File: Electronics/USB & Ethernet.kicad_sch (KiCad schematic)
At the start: 13 parts, among them IC4 USB2512B-AEZG, J24 USB_A_Stacked, Y3 30MHz

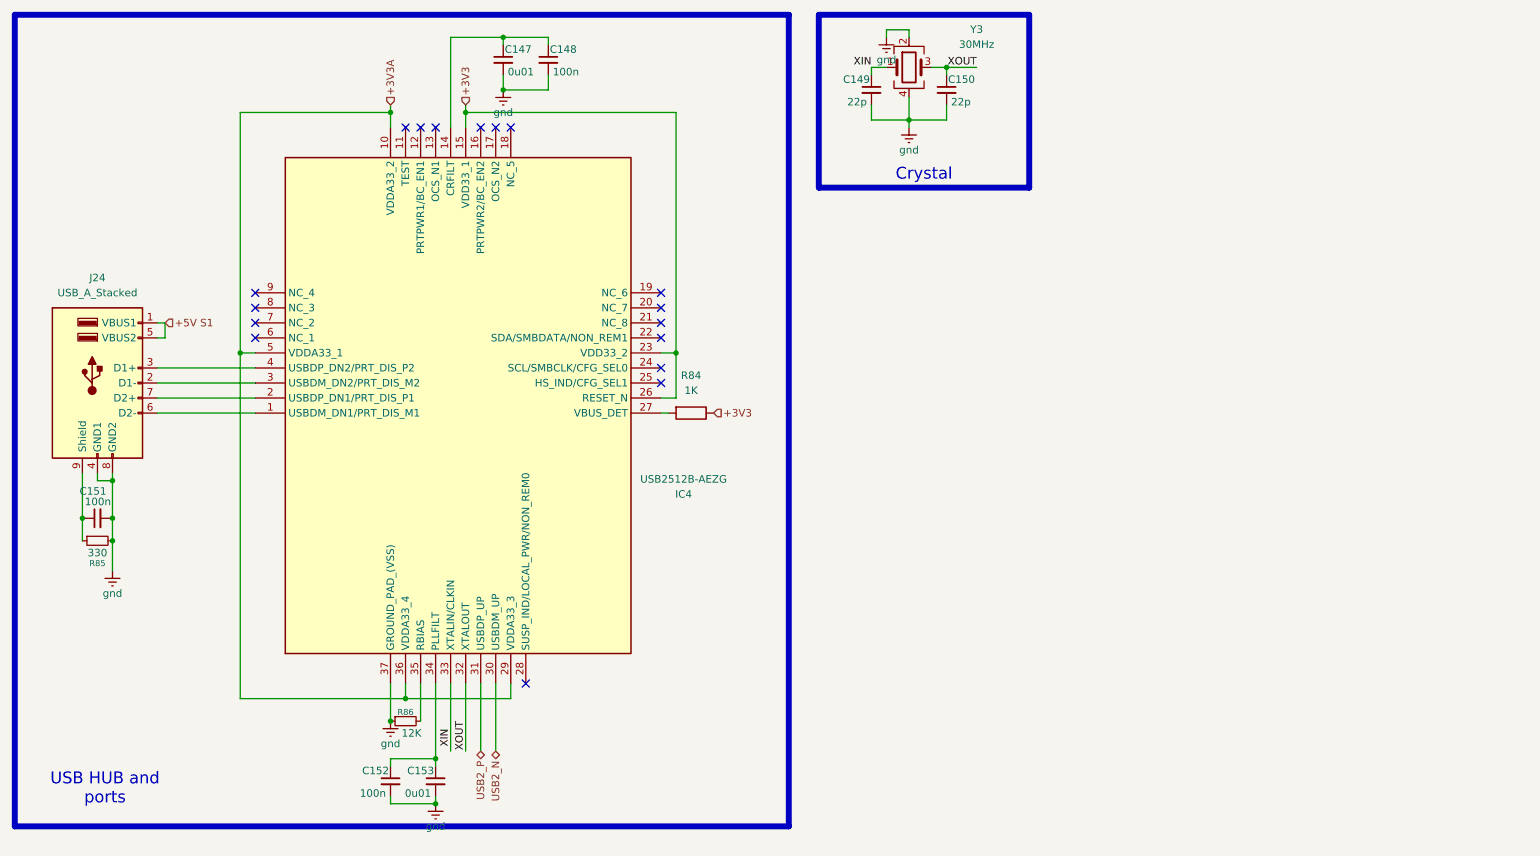
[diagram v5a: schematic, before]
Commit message: Sata Port Changed
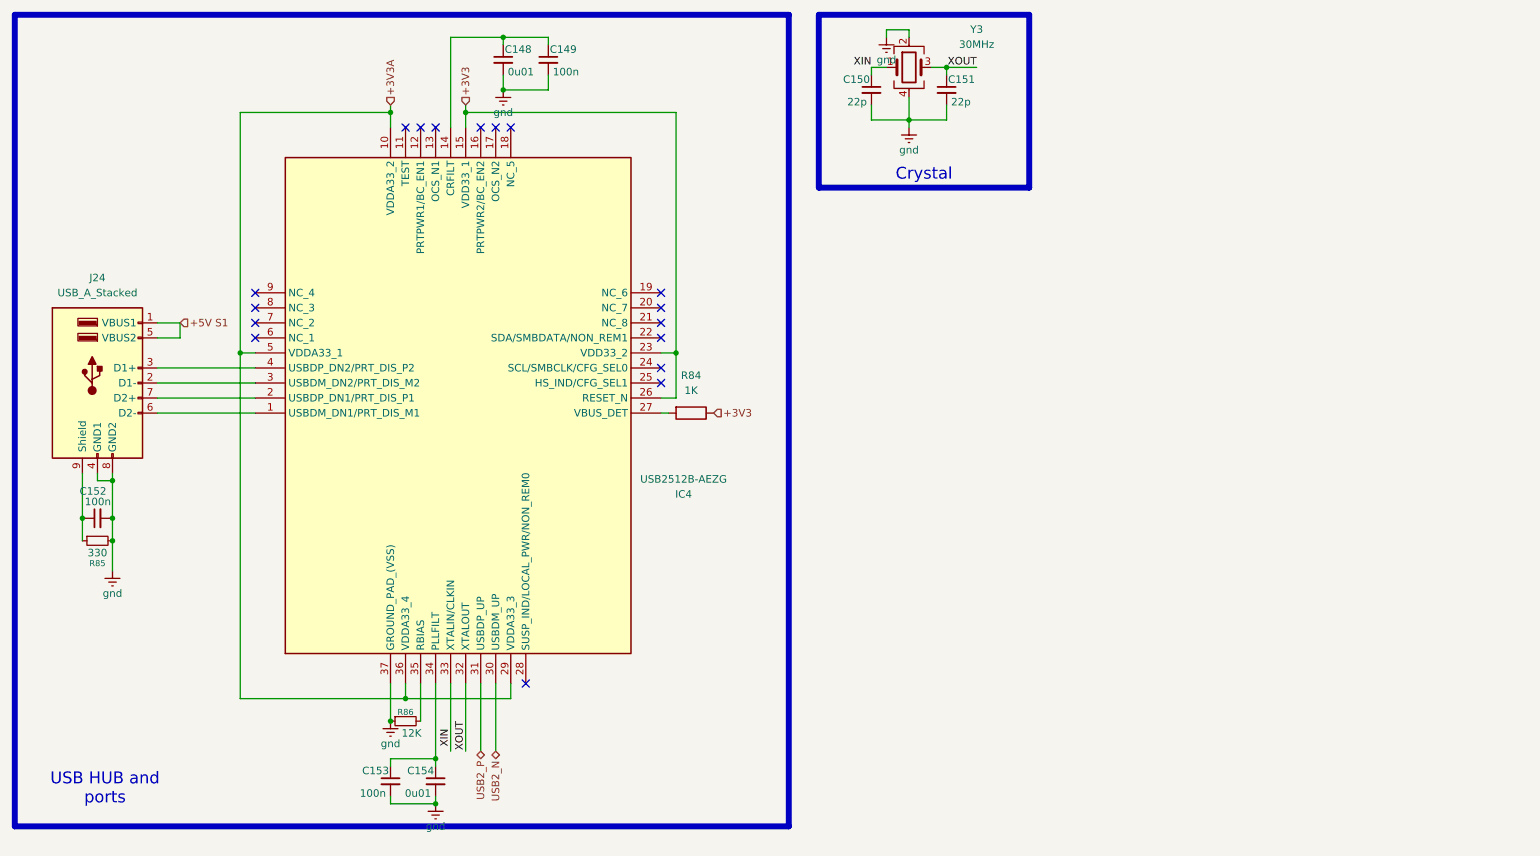
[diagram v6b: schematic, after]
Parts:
- renumbered C147 to C148, C148 to C149, C149 to C150, C150 to C151, C151 to C152, C152 to C153, C153 to C154
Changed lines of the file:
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@@
 	(wire
 		(pts
-			(xy 39.37 69.85) (xy 40.64 69.85)
+			(xy 43.18 69.85) (xy 43.18 67.31)
+		)
+		(stroke
+			(width 0)
+			(type default)
+		)
+	)
+	(wire
+		(pts
+			(xy 39.37 69.85) (xy 43.18 69.85)
 		)
 		(stroke
@@
 	(wire
 		(pts
-			(xy 40.64 67.31) (xy 39.37 67.31)
-		)
-		(stroke
-			(width 0)
-			(type default)
-		)
-	)
-	(wire
-		(pts
 			(xy 166.37 33.02) (xy 172.72 33.02)
 		)
@@
 	(wire
 		(pts
-			(xy 40.64 69.85) (xy 40.64 67.31)
-		)
-		(stroke
-			(width 0)
-			(type default)
-		)
-	)
-	(wire
-		(pts
 			(xy 88.9 128.27) (xy 88.9 139.7)
 		)
@@
 		(pts
 			(xy 97.79 25.4) (xy 97.79 27.94)
+		)
+		(stroke
+			(width 0)
+			(type default)
+		)
+	)
+	(wire
+		(pts
+			(xy 43.18 67.31) (xy 39.37 67.31)
 		)
 		(stroke
@@
 	(hierarchical_label "+5V S1"
 		(shape input)
-		(at 40.64 67.31 0)
+		(at 43.18 67.31 0)
 		(effects
 			(font
@@
 			)
 			(justify right)
+		)
+	)
+	(netclass_flag ""
+		(length 2.54)
+		(shape round)
+		(at 53.34 31.75 0)
+		(fields_autoplaced yes)
+		(effects
+			(font
+				(size 1.27 1.27)
+			)
+			(justify left bottom)
+		)
+		(property "Netclass" "PWR RAIL"
+			(at 54.0385 29.21 0)
+			(effects
+				(font
+					(size 1.27 1.27)
+				)
+				(justify left)
+			)
+		)
+		(property "Component Class" ""
+			(at -344.17 -53.34 0)
+			(effects
+				(font
+					(size 1.27 1.27)
+					(italic yes)
+				)
+			)
+		)
+	)
+	(netclass_flag ""
+		(length 2.54)
+		(shape round)
+		(at 43.18 69.85 180)
+		(fields_autoplaced yes)
+		(effects
+			(font
+				(size 1.27 1.27)
+			)
+			(justify right bottom)
+		)
+		(property "Netclass" "PWR RAIL"
+			(at 43.8785 72.39 0)
+			(effects
+				(font
+					(size 1.27 1.27)
+				)
+				(justify left)
+			)
+		)
+		(property "Component Class" ""
+			(at -354.33 154.94 0)
+			(effects
+				(font
+					(size 1.27 1.27)
+					(italic yes)
+				)
+			)
+		)
+	)
+	(netclass_flag ""
+		(length 2.54)
+		(shape round)
+		(at 127 31.75 0)
+		(fields_autoplaced yes)
+		(effects
+			(font
+				(size 1.27 1.27)
+			)
+			(justify left bottom)
+		)
+		(property "Netclass" "PWR RAIL"
+			(at 126.3015 29.21 0)
+			(effects
+				(font
+					(size 1.27 1.27)
+				)
+				(justify right)
+			)
+		)
+		(property "Component Class" ""
+			(at 524.51 -53.34 0)
+			(effects
+				(font
+					(size 1.27 1.27)
+					(italic yes)
+				)
+				(justify left)
+			)
 		)
 	)
@@
 		(on_board yes)
 		(dnp no)
-		(property "Reference" "#PWR0167"
+		(property "Reference" "#PWR0169"
 			(at 97.79 34.29 0)
 			(effects
@@
 			(project "CM5 Nas"
 				(path "/0650c7a8-acba-429c-9f8e-eec0baf0bc1c/fede4c36-00cc-4d3d-b71c-5243ba232202/6a9d58eb-7efc-489b-8392-0909cd6b0d5f"
-					(reference "#PWR0167")
+					(reference "#PWR0169")
 					(unit 1)
 				)
@@
 		(on_board yes)
 		(dnp no)
-		(property "Reference" "C153"
+		(property "Reference" "C154"
 			(at 86.106 143.002 0)
 			(effects
@@
 			(project "CM5 Nas"
 				(path "/0650c7a8-acba-429c-9f8e-eec0baf0bc1c/fede4c36-00cc-4d3d-b71c-5243ba232202/6a9d58eb-7efc-489b-8392-0909cd6b0d5f"
-					(reference "C153")
+					(reference "C154")
 					(unit 1)
 				)
@@
 		(on_board yes)
 		(dnp no)
-		(property "Reference" "C152"
+		(property "Reference" "C153"
 			(at 78.486 143.002 0)
 			(effects
@@
 			(project "CM5 Nas"
 				(path "/0650c7a8-acba-429c-9f8e-eec0baf0bc1c/fede4c36-00cc-4d3d-b71c-5243ba232202/6a9d58eb-7efc-489b-8392-0909cd6b0d5f"
-					(reference "C152")
+					(reference "C153")
 					(unit 1)
 				)
@@
 		(on_board yes)
 		(dnp no)
-		(property "Reference" "C150"
+		(property "Reference" "C151"
 			(at 172.974 26.162 0)
 			(effects
@@
 			(project "CM5 Nas"
 				(path "/0650c7a8-acba-429c-9f8e-eec0baf0bc1c/fede4c36-00cc-4d3d-b71c-5243ba232202/6a9d58eb-7efc-489b-8392-0909cd6b0d5f"
-					(reference "C150")
+					(reference "C151")
 					(unit 1)
 				)
@@
 		(on_board yes)
 		(dnp no)
-		(property "Reference" "C147"
+		(property "Reference" "C148"
 			(at 98.044 21.082 0)
 			(effects
@@
 			(project "CM5 Nas"
 				(path "/0650c7a8-acba-429c-9f8e-eec0baf0bc1c/fede4c36-00cc-4d3d-b71c-5243ba232202/6a9d58eb-7efc-489b-8392-0909cd6b0d5f"
-					(reference "C147")
+					(reference "C148")
 					(unit 1)
 				)
@@
 		(on_board yes)
 		(dnp no)
-		(property "Reference" "#PWR0166"
+		(property "Reference" "#PWR0168"
 			(at 162.56 25.4 0)
 			(effects
@@
 			(project "CM5 Nas"
 				(path "/0650c7a8-acba-429c-9f8e-eec0baf0bc1c/fede4c36-00cc-4d3d-b71c-5243ba232202/6a9d58eb-7efc-489b-8392-0909cd6b0d5f"
-					(reference "#PWR0166")
+					(reference "#PWR0168")
 					(unit 1)
 				)
@@
 		(on_board yes)
 		(dnp no)
-		(property "Reference" "#PWR0168"
+		(property "Reference" "#PWR0170"
 			(at 166.37 40.64 0)
 			(effects
@@
 			(project "CM5 Nas"
 				(path "/0650c7a8-acba-429c-9f8e-eec0baf0bc1c/fede4c36-00cc-4d3d-b71c-5243ba232202/6a9d58eb-7efc-489b-8392-0909cd6b0d5f"
-					(reference "#PWR0168")
+					(reference "#PWR0170")
 					(unit 1)
 				)
@@
 		(on_board yes)
 		(dnp no)
-		(property "Reference" "#PWR0171"
+		(property "Reference" "#PWR0173"
 			(at 86.36 154.94 0)
 			(effects
@@
 			(project "CM5 Nas"
 				(path "/0650c7a8-acba-429c-9f8e-eec0baf0bc1c/fede4c36-00cc-4d3d-b71c-5243ba232202/6a9d58eb-7efc-489b-8392-0909cd6b0d5f"
-					(reference "#PWR0171")
+					(reference "#PWR0173")
 					(unit 1)
 				)
@@
 		(on_board yes)
 		(dnp no)
-		(property "Reference" "C148"
+		(property "Reference" "C149"
 			(at 105.664 21.082 0)
 			(effects
@@
 			(project "CM5 Nas"
 				(path "/0650c7a8-acba-429c-9f8e-eec0baf0bc1c/fede4c36-00cc-4d3d-b71c-5243ba232202/6a9d58eb-7efc-489b-8392-0909cd6b0d5f"
-					(reference "C148")
+					(reference "C149")
 					(unit 1)
 				)
@@
 		(on_board yes)
 		(dnp no)
-		(property "Reference" "#PWR0169"
+		(property "Reference" "#PWR0171"
 			(at 31.75 115.57 0)
 			(effects
@@
 			(project "CM5 Nas"
 				(path "/0650c7a8-acba-429c-9f8e-eec0baf0bc1c/fede4c36-00cc-4d3d-b71c-5243ba232202/6a9d58eb-7efc-489b-8392-0909cd6b0d5f"
-					(reference "#PWR0169")
+					(reference "#PWR0171")
 					(unit 1)
 				)
@@
 		(on_board yes)
 		(dnp no)
-		(property "Reference" "#PWR0170"
+		(property "Reference" "#PWR0172"
 			(at 78.74 140.97 0)
 			(effects
@@
 			(project "CM5 Nas"
 				(path "/0650c7a8-acba-429c-9f8e-eec0baf0bc1c/fede4c36-00cc-4d3d-b71c-5243ba232202/6a9d58eb-7efc-489b-8392-0909cd6b0d5f"
-					(reference "#PWR0170")
+					(reference "#PWR0172")
 					(unit 1)
 				)
@@
 		(on_board yes)
 		(dnp no)
-		(property "Reference" "C151"
+		(property "Reference" "C152"
 			(at 30.734 95.758 90)
 			(effects
@@
 			(project "CM5 Nas"
 				(path "/0650c7a8-acba-429c-9f8e-eec0baf0bc1c/fede4c36-00cc-4d3d-b71c-5243ba232202/6a9d58eb-7efc-489b-8392-0909cd6b0d5f"
-					(reference "C151")
+					(reference "C152")
 					(unit 1)
 				)
@@
 		(on_board yes)
 		(dnp no)
-		(property "Reference" "C149"
+		(property "Reference" "C150"
 			(at 159.766 26.162 0)
 			(effects
@@
 			(project "CM5 Nas"
 				(path "/0650c7a8-acba-429c-9f8e-eec0baf0bc1c/fede4c36-00cc-4d3d-b71c-5243ba232202/6a9d58eb-7efc-489b-8392-0909cd6b0d5f"
-					(reference "C149")
+					(reference "C150")
 					(unit 1)
 				)

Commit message: Changed sata port
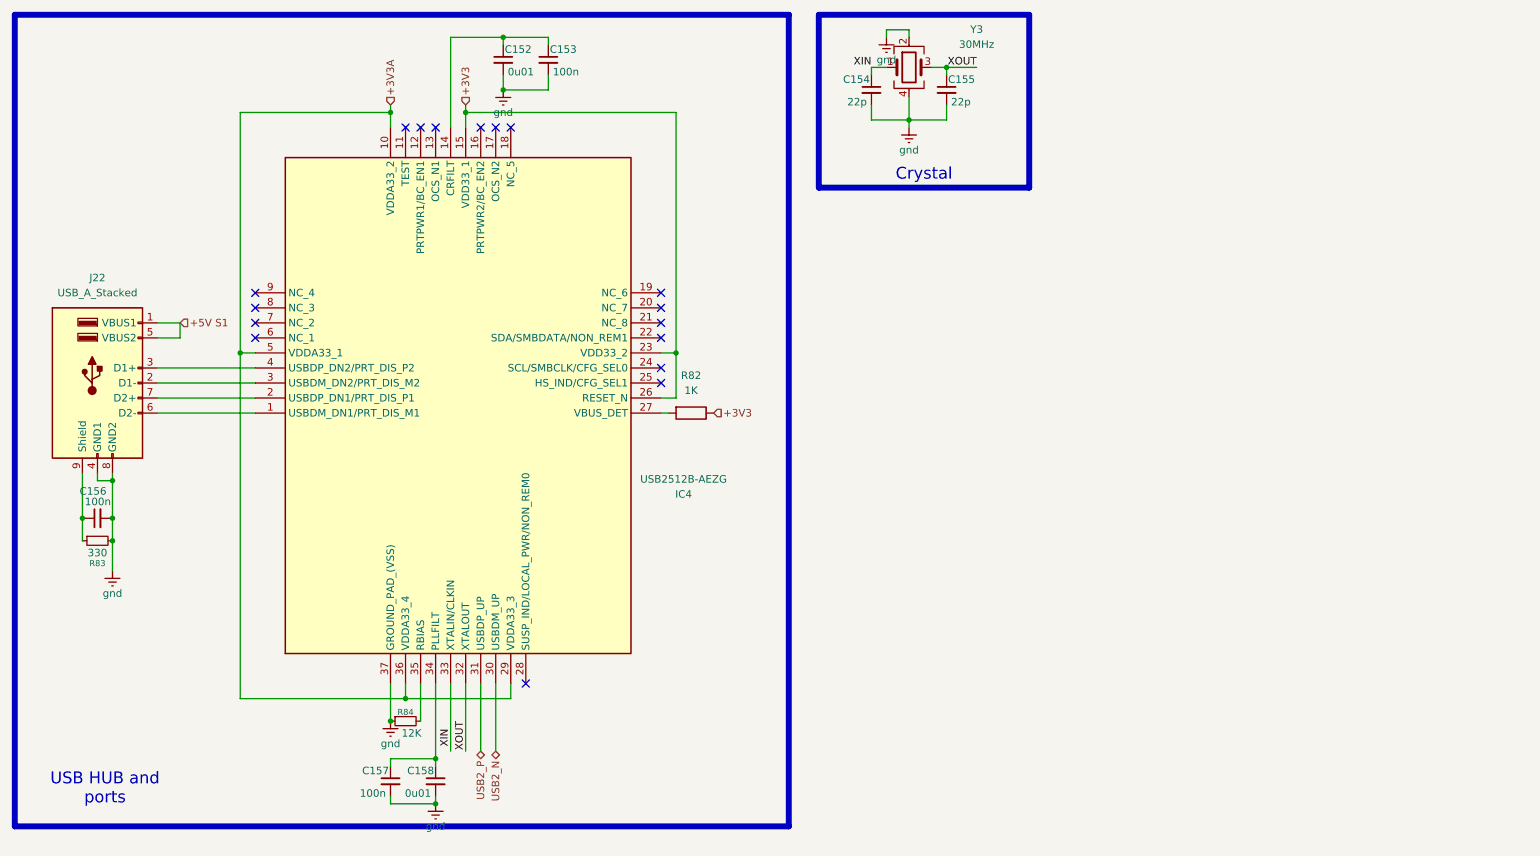
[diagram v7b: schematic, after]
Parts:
- renumbered C148 to C152, C149 to C153, C150 to C154, C151 to C155, C152 to C156, C153 to C157, C154 to C158, J24 to J22, R84 to R82, R85 to R83, R86 to R84
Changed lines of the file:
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@@
 		(on_board yes)
 		(dnp no)
-		(property "Reference" "#PWR0169"
+		(property "Reference" "#PWR0163"
 			(at 97.79 34.29 0)
 			(effects
@@
 			(project "CM5 Nas"
 				(path "/0650c7a8-acba-429c-9f8e-eec0baf0bc1c/fede4c36-00cc-4d3d-b71c-5243ba232202/6a9d58eb-7efc-489b-8392-0909cd6b0d5f"
-					(reference "#PWR0169")
+					(reference "#PWR0163")
 					(unit 1)
 				)
@@
 		(on_board yes)
 		(dnp no)
-		(property "Reference" "C154"
+		(property "Reference" "C158"
 			(at 86.106 143.002 0)
 			(effects
@@
 			(project "CM5 Nas"
 				(path "/0650c7a8-acba-429c-9f8e-eec0baf0bc1c/fede4c36-00cc-4d3d-b71c-5243ba232202/6a9d58eb-7efc-489b-8392-0909cd6b0d5f"
-					(reference "C154")
+					(reference "C158")
 					(unit 1)
 				)
@@
 		(dnp no)
 		(fields_autoplaced yes)
-		(property "Reference" "J24"
+		(property "Reference" "J22"
 			(at 29.21 59.69 0)
 			(effects
@@
 			(project ""
 				(path "/0650c7a8-acba-429c-9f8e-eec0baf0bc1c/fede4c36-00cc-4d3d-b71c-5243ba232202/6a9d58eb-7efc-489b-8392-0909cd6b0d5f"
-					(reference "J24")
+					(reference "J22")
 					(unit 1)
 				)
@@
 		(on_board yes)
 		(dnp no)
-		(property "Reference" "C153"
+		(property "Reference" "C157"
 			(at 78.486 143.002 0)
 			(effects
@@
 			(project "CM5 Nas"
 				(path "/0650c7a8-acba-429c-9f8e-eec0baf0bc1c/fede4c36-00cc-4d3d-b71c-5243ba232202/6a9d58eb-7efc-489b-8392-0909cd6b0d5f"
-					(reference "C153")
+					(reference "C157")
 					(unit 1)
 				)
@@
 		(on_board yes)
 		(dnp no)
-		(property "Reference" "R85"
+		(property "Reference" "R83"
 			(at 29.21 107.95 90)
 			(effects
@@
 			(project "CM5 Nas"
 				(path "/0650c7a8-acba-429c-9f8e-eec0baf0bc1c/fede4c36-00cc-4d3d-b71c-5243ba232202/6a9d58eb-7efc-489b-8392-0909cd6b0d5f"
-					(reference "R85")
+					(reference "R83")
 					(unit 1)
 				)
@@
 		(on_board yes)
 		(dnp no)
-		(property "Reference" "C151"
+		(property "Reference" "C155"
 			(at 172.974 26.162 0)
 			(effects
@@
 			(project "CM5 Nas"
 				(path "/0650c7a8-acba-429c-9f8e-eec0baf0bc1c/fede4c36-00cc-4d3d-b71c-5243ba232202/6a9d58eb-7efc-489b-8392-0909cd6b0d5f"
-					(reference "C151")
+					(reference "C155")
 					(unit 1)
 				)
@@
 		(on_board yes)
 		(dnp no)
-		(property "Reference" "C148"
+		(property "Reference" "C152"
 			(at 98.044 21.082 0)
 			(effects
@@
 			(project "CM5 Nas"
 				(path "/0650c7a8-acba-429c-9f8e-eec0baf0bc1c/fede4c36-00cc-4d3d-b71c-5243ba232202/6a9d58eb-7efc-489b-8392-0909cd6b0d5f"
-					(reference "C148")
+					(reference "C152")
 					(unit 1)
 				)
@@
 		(on_board yes)
 		(dnp no)
-		(property "Reference" "#PWR0168"
+		(property "Reference" "#PWR0162"
 			(at 162.56 25.4 0)
 			(effects
@@
 			(project "CM5 Nas"
 				(path "/0650c7a8-acba-429c-9f8e-eec0baf0bc1c/fede4c36-00cc-4d3d-b71c-5243ba232202/6a9d58eb-7efc-489b-8392-0909cd6b0d5f"
-					(reference "#PWR0168")
+					(reference "#PWR0162")
 					(unit 1)
 				)
@@
 		(on_board yes)
 		(dnp no)
-		(property "Reference" "#PWR0170"
+		(property "Reference" "#PWR0164"
 			(at 166.37 40.64 0)
 			(effects
@@
 			(project "CM5 Nas"
 				(path "/0650c7a8-acba-429c-9f8e-eec0baf0bc1c/fede4c36-00cc-4d3d-b71c-5243ba232202/6a9d58eb-7efc-489b-8392-0909cd6b0d5f"
-					(reference "#PWR0170")
+					(reference "#PWR0164")
 					(unit 1)
 				)
@@
 		(on_board yes)
 		(dnp no)
-		(property "Reference" "#PWR0173"
+		(property "Reference" "#PWR0167"
 			(at 86.36 154.94 0)
 			(effects
@@
 			(project "CM5 Nas"
 				(path "/0650c7a8-acba-429c-9f8e-eec0baf0bc1c/fede4c36-00cc-4d3d-b71c-5243ba232202/6a9d58eb-7efc-489b-8392-0909cd6b0d5f"
-					(reference "#PWR0173")
+					(reference "#PWR0167")
 					(unit 1)
 				)
@@
 		(on_board yes)
 		(dnp no)
-		(property "Reference" "C149"
+		(property "Reference" "C153"
 			(at 105.664 21.082 0)
 			(effects
@@
 			(project "CM5 Nas"
 				(path "/0650c7a8-acba-429c-9f8e-eec0baf0bc1c/fede4c36-00cc-4d3d-b71c-5243ba232202/6a9d58eb-7efc-489b-8392-0909cd6b0d5f"
-					(reference "C149")
+					(reference "C153")
 					(unit 1)
 				)
@@
 		(on_board yes)
 		(dnp no)
-		(property "Reference" "R86"
+		(property "Reference" "R84"
 			(at 81.28 133.096 90)
 			(effects
@@
 			(project ""
 				(path "/0650c7a8-acba-429c-9f8e-eec0baf0bc1c/fede4c36-00cc-4d3d-b71c-5243ba232202/6a9d58eb-7efc-489b-8392-0909cd6b0d5f"
-					(reference "R86")
+					(reference "R84")
 					(unit 1)
 				)
@@
 		(on_board yes)
 		(dnp no)
-		(property "Reference" "#PWR0171"
+		(property "Reference" "#PWR0165"
 			(at 31.75 115.57 0)
 			(effects
@@
 			(project "CM5 Nas"
 				(path "/0650c7a8-acba-429c-9f8e-eec0baf0bc1c/fede4c36-00cc-4d3d-b71c-5243ba232202/6a9d58eb-7efc-489b-8392-0909cd6b0d5f"
-					(reference "#PWR0171")
+					(reference "#PWR0165")
 					(unit 1)
 				)
@@
 		(on_board yes)
 		(dnp no)
-		(property "Reference" "#PWR0172"
+		(property "Reference" "#PWR0166"
 			(at 78.74 140.97 0)
 			(effects
@@
 			(project "CM5 Nas"
 				(path "/0650c7a8-acba-429c-9f8e-eec0baf0bc1c/fede4c36-00cc-4d3d-b71c-5243ba232202/6a9d58eb-7efc-489b-8392-0909cd6b0d5f"
-					(reference "#PWR0172")
+					(reference "#PWR0166")
 					(unit 1)
 				)
@@
 		(dnp no)
 		(fields_autoplaced yes)
-		(property "Reference" "R84"
+		(property "Reference" "R82"
 			(at 129.54 76.2 90)
 			(effects
@@
 			(project ""
 				(path "/0650c7a8-acba-429c-9f8e-eec0baf0bc1c/fede4c36-00cc-4d3d-b71c-5243ba232202/6a9d58eb-7efc-489b-8392-0909cd6b0d5f"
-					(reference "R84")
+					(reference "R82")
 					(unit 1)
 				)
@@
 		(on_board yes)
 		(dnp no)
-		(property "Reference" "C152"
+		(property "Reference" "C156"
 			(at 30.734 95.758 90)
 			(effects
@@
 			(project "CM5 Nas"
 				(path "/0650c7a8-acba-429c-9f8e-eec0baf0bc1c/fede4c36-00cc-4d3d-b71c-5243ba232202/6a9d58eb-7efc-489b-8392-0909cd6b0d5f"
-					(reference "C152")
+					(reference "C156")
 					(unit 1)
 				)
@@
 		(on_board yes)
 		(dnp no)
-		(property "Reference" "C150"
+		(property "Reference" "C154"
 			(at 159.766 26.162 0)
 			(effects
@@
 			(project "CM5 Nas"
 				(path "/0650c7a8-acba-429c-9f8e-eec0baf0bc1c/fede4c36-00cc-4d3d-b71c-5243ba232202/6a9d58eb-7efc-489b-8392-0909cd6b0d5f"
-					(reference "C150")
-					(unit 1)
-				)
+					(reference "C154")
+					(unit 1)
+				)
